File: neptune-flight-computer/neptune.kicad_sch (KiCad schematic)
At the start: 0 parts

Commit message: Continued work on board
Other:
- sheet RF renamed Data management
- added sheet STM32 (STM32.kicad_sch)
- added sheet Sensors (Sensors.kicad_sch)
- sheet Data management: file RF.kicad_sch -> data_management.kicad_sch

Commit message: Added oscillator, setup sensor SPI
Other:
- sheet Sensors ports: added CE_ACC, CE_GYR, CE_MAG, IMU_MISO, IMU_MOSI, IMU_SCK; removed BMX_Int_1, SCL, SDA
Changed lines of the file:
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@@
 (kicad_sch (version 20211123) (generator eeschema)
   (paper "A4")
+  (wire (pts (xy 241.3 35.56) (xy 245.11 35.56))
+    (stroke (width 0) (type default) (color 0 0 0 0))
+  )
+  (wire (pts (xy 241.3 46.99) (xy 245.11 46.99))
+    (stroke (width 0) (type default) (color 0 0 0 0))
+  )
+  (wire (pts (xy 241.3 50.8) (xy 245.11 50.8))
+    (stroke (width 0) (type default) (color 0 0 0 0))
+  )
+  (wire (pts (xy 241.3 39.37) (xy 245.11 39.37))
+    (stroke (width 0) (type default) (color 0 0 0 0))
+  )
+  (wire (pts (xy 241.3 43.18) (xy 245.11 43.18))
+    (stroke (width 0) (type default) (color 0 0 0 0))
+  )
+  (wire (pts (xy 241.3 31.75) (xy 245.11 31.75))
+    (stroke (width 0) (type default) (color 0 0 0 0))
+  )
+  (label "IMU_SCK" (at 245.11 50.8 0)
+    (effects (font (size 1.27 1.27)) (justify left bottom))
+  )
+  (label "CE_ACC" (at 245.11 35.56 0)
+    (effects (font (size 1.27 1.27)) (justify left bottom))
+  )
+  (label "IMU_MISO" (at 245.11 43.18 0)
+    (effects (font (size 1.27 1.27)) (justify left bottom))
+  )
+  (label "IMU_MOSI" (at 245.11 46.99 0)
+    (effects (font (size 1.27 1.27)) (justify left bottom))
+  )
+  (label "CE_MAG" (at 245.11 39.37 0)
+    (effects (font (size 1.27 1.27)) (justify left bottom))
+  )
+  (label "CE_GYR" (at 245.11 31.75 0)
+    (effects (font (size 1.27 1.27)) (justify left bottom))
+  )
   (sheet (at 25.4 88.9) (size 63.5 50.8) (fields_autoplaced)
     (stroke (width 0.1524) (type solid) (color 0 0 0 0))
@@
       (effects (font (size 1.27 1.27)) (justify left top))
     )
-    (pin "SCL" input (at 241.3 33.02 0)
-      (effects (font (size 1.27 1.27)) (justify right))
-    )
-    (pin "SDA" input (at 241.3 36.83 0)
-      (effects (font (size 1.27 1.27)) (justify right))
-    )
-    (pin "BMX_Int_1" input (at 241.3 40.64 0)
+    (pin "CE_GYR" input (at 241.3 31.75 0)
+      (effects (font (size 1.27 1.27)) (justify right))
+    )
+    (pin "CE_ACC" input (at 241.3 35.56 0)
+      (effects (font (size 1.27 1.27)) (justify right))
+    )
+    (pin "CE_MAG" input (at 241.3 39.37 0)
+      (effects (font (size 1.27 1.27)) (justify right))
+    )
+    (pin "IMU_MISO" output (at 241.3 43.18 0)
+      (effects (font (size 1.27 1.27)) (justify right))
+    )
+    (pin "IMU_SCK" input (at 241.3 50.8 0)
+      (effects (font (size 1.27 1.27)) (justify right))
+    )
+    (pin "IMU_MOSI" input (at 241.3 46.99 0)
       (effects (font (size 1.27 1.27)) (justify right))
     )
@@
       (reference "#PWR?") (unit 1) (value "GND") (footprint "")
     )
+    (path "/708c8a34-f258-4554-8b50-7818f1e46fec/1c76a57f-6fd0-487a-a4ef-6ad233efc7a4"
+      (reference "#PWR?") (unit 1) (value "GND") (footprint "")
+    )
     (path "/b694d9b6-8e2a-4217-a81b-e156ec88b46a/1e295ccf-d58f-4d56-9b3f-857eee3b562a"
       (reference "#PWR?") (unit 1) (value "GND") (footprint "")
@@
       (reference "#PWR?") (unit 1) (value "GND") (footprint "")
     )
+    (path "/708c8a34-f258-4554-8b50-7818f1e46fec/49ef88cf-fbc5-444e-b0de-982ad307474e"
+      (reference "#PWR?") (unit 1) (value "+5V") (footprint "")
+    )
+    (path "/708c8a34-f258-4554-8b50-7818f1e46fec/4b6825c9-a1f7-4ead-9756-29ea3c3b647a"
+      (reference "#PWR?") (unit 1) (value "GND") (footprint "")
+    )
     (path "/708c8a34-f258-4554-8b50-7818f1e46fec/60e7330f-4ecb-47a7-a6a7-dc5a9900bcfe"
       (reference "#PWR?") (unit 1) (value "+3.3V") (footprint "")
@@
       (reference "#PWR?") (unit 1) (value "GND") (footprint "")
     )
+    (path "/fd0daead-056b-49b0-b136-e76d44737a4c/64ccf757-c39c-4a22-ae39-be2ebf19a906"
+      (reference "#PWR?") (unit 1) (value "GND") (footprint "")
+    )
     (path "/fd0daead-056b-49b0-b136-e76d44737a4c/68003f26-a4e5-4ffc-8df9-5c391f729a97"
       (reference "#PWR?") (unit 1) (value "+3.3V") (footprint "")
@@
       (reference "#PWR?") (unit 1) (value "GND") (footprint "")
     )
-    (path "/fd0daead-056b-49b0-b136-e76d44737a4c/9780d6ee-b4a2-44ea-907d-1bb30473759e"
+    (path "/708c8a34-f258-4554-8b50-7818f1e46fec/a23244bc-53f6-42d4-9bec-2b4f35d62696"
       (reference "#PWR?") (unit 1) (value "GND") (footprint "")
     )
     (path "/761c8e29-382a-475c-a37a-7201cc9cd0f5/a470ca0b-2a36-4daa-901d-3247fe3e860c"
+      (reference "#PWR?") (unit 1) (value "GND") (footprint "")
+    )
+    (path "/708c8a34-f258-4554-8b50-7818f1e46fec/a51b5ced-5450-4509-900e-2b4a4f5469b4"
       (reference "#PWR?") (unit 1) (value "GND") (footprint "")
     )
@@
       (reference "#PWR?") (unit 1) (value "GND") (footprint "")
     )
+    (path "/708c8a34-f258-4554-8b50-7818f1e46fec/ce55234b-9d12-40d9-8108-46d3eb66f17c"
+      (reference "#PWR?") (unit 1) (value "+5V") (footprint "")
+    )
     (path "/761c8e29-382a-475c-a37a-7201cc9cd0f5/d2a988e4-3734-4b36-a333-4fd6c96f76ed"
       (reference "#PWR?") (unit 1) (value "VBUS") (footprint "")
@@
       (reference "#PWR?") (unit 1) (value "GND") (footprint "")
     )
-    (path "/fd0daead-056b-49b0-b136-e76d44737a4c/d8e3e689-c509-4bd8-b960-1bb37ee4f3bd"
-      (reference "#PWR?") (unit 1) (value "GND") (footprint "")
-    )
     (path "/708c8a34-f258-4554-8b50-7818f1e46fec/dcce9beb-a6a5-4ab2-8739-7a753559b830"
       (reference "#PWR?") (unit 1) (value "VBUS") (footprint "")
@@
       (reference "C?") (unit 1) (value "8.2n") (footprint "Capacitor_SMD:C_0402_1005Metric")
     )
+    (path "/708c8a34-f258-4554-8b50-7818f1e46fec/86e4c295-0c0b-45dc-a306-ca91d6b44a72"
+      (reference "C?") (unit 1) (value "33p") (footprint "Capacitor_SMD:C_0402_1005Metric")
+    )
     (path "/761c8e29-382a-475c-a37a-7201cc9cd0f5/877c3fb5-6549-4ea3-9af6-a23063a08a80"
       (reference "C?") (unit 1) (value "10u") (footprint "Capacitor_SMD:C_0805_2012Metric_Pad1.18x1.45mm_HandSolder")
     )
+    (path "/708c8a34-f258-4554-8b50-7818f1e46fec/9e179446-9863-4cc8-a0d5-4367254f4d3e"
+      (reference "C?") (unit 1) (value "33p") (footprint "Capacitor_SMD:C_0402_1005Metric")
+    )
     (path "/761c8e29-382a-475c-a37a-7201cc9cd0f5/bf1a3858-9fb0-46de-bab4-bd386edc9d50"
       (reference "C?") (unit 1) (value "1u") (footprint "Capacitor_SMD:C_0402_1005Metric")
@@
       (reference "J?") (unit 1) (value "Conn_Coaxial") (footprint "Connector_Coaxial:SMA_Amphenol_132291_Vertical")
     )
+    (path "/708c8a34-f258-4554-8b50-7818f1e46fec/b33b18f8-aa94-4a60-bf88-916bdc3ca6d3"
+      (reference "J?") (unit 1) (value "Conn_01x04") (footprint "Connector_PinHeader_2.54mm:PinHeader_1x04_P2.54mm_Vertical")
+    )
+    (path "/708c8a34-f258-4554-8b50-7818f1e46fec/c58efe95-928d-4eed-a2d1-8d8e37e3e668"
+      (reference "J?") (unit 1) (value "Conn_01x04") (footprint "Connector_PinHeader_2.54mm:PinHeader_1x04_P2.54mm_Vertical")
+    )
     (path "/708c8a34-f258-4554-8b50-7818f1e46fec/c6de421b-8d8f-4889-9433-957986658d20"
-      (reference "J?") (unit 1) (value "Conn_01x04") (footprint "footprints:JST_SM04B-GHS-TB(LF)(SN)-")
+      (reference "J?") (unit 1) (value "Conn_01x04") (footprint "Connector_PinHeader_2.54mm:PinHeader_1x04_P2.54mm_Vertical")
     )
     (path "/761c8e29-382a-475c-a37a-7201cc9cd0f5/d8f6b77f-bde2-4824-b9e2-53c92a41d9c6"
@@
       (reference "U?") (unit 3) (value "LM393") (footprint "footprints:SOIC127P600X175-8N")
     )
-  )
+    (path "/708c8a34-f258-4554-8b50-7818f1e46fec/16719f82-68bb-4f6d-a5e9-cdc1fab5beb3"
+      (reference "Y?") (unit 1) (value "Crystal") (footprint "Crystal:Crystal_SMD_HC49-SD")
+    )
+  )

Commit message: Continued pcb work
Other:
- sheet Data management ports: added CLK_SD, CS_RF, CS_SD, MISO_RF, MISO_SD, MOSI_RF, MOSI_SD, RESET_RF, RF_IO0, SCK_RF; removed none
- sheet STM32 ports: added CE_ACC, CE_GYR, CE_MAG, CLK_SD, CS_RF, CS_SD, IMU_MISO, IMU_MOSI, IMU_SCK, MISO_RF, MISO_SD, MOSI_RF, MOSI_SD, RESET_RF, RF_100, SCK_RF; removed none

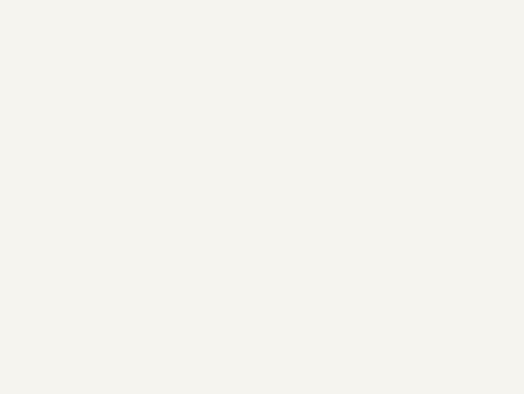
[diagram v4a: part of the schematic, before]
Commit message: Added mounting holes
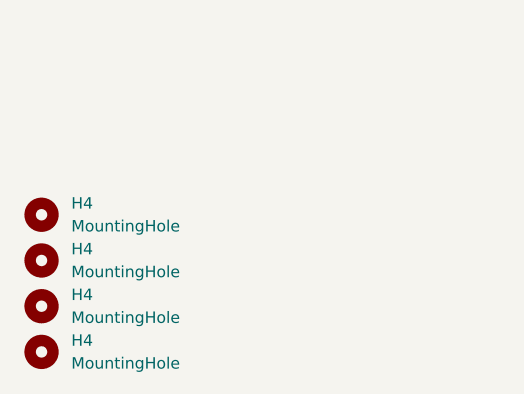
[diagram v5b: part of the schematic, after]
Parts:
- added H4 (x4): MountingHole, MountingHole:MountingHole_3.2mm_M3, symbol Mechanical:MountingHole
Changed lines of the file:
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@@
     (effects (font (size 1.27 1.27)) (justify left bottom))
+  )
+  (symbol (lib_id "Mechanical:MountingHole") (at 27.94 175.26 0) (unit 1)
+    (in_bom yes) (on_board yes) (dnp no) (fields_autoplaced)
+    (property "Reference" "H4" (at 31.242 173.9899 0)
+      (effects (font (size 1.27 1.27)) (justify left))
+    )
+    (property "Value" "MountingHole" (at 31.242 176.5299 0)
+      (effects (font (size 1.27 1.27)) (justify left))
+    )
+    (property "Footprint" "MountingHole:MountingHole_3.2mm_M3" (at 27.94 175.26 0)
+      (effects (font (size 1.27 1.27)) hide)
+    )
+    (property "Datasheet" "~" (at 27.94 175.26 0)
+      (effects (font (size 1.27 1.27)) hide)
+    )
+    (instances
+      (project "Liaka_V3"
+        (path "/9186fd02-f30d-4e17-aa38-378ab73e3908"
+          (reference "H4") (unit 1)
+        )
+      )
+      (project "neptune"
+        (path "/e63e39d7-6ac0-4ffd-8aa3-1841a4541b55"
+          (reference "H2") (unit 1)
+        )
+      )
+    )
+  )
+  (symbol (lib_id "Mechanical:MountingHole") (at 27.94 180.34 0) (unit 1)
+    (in_bom yes) (on_board yes) (dnp no) (fields_autoplaced)
+    (property "Reference" "H4" (at 31.242 179.0699 0)
+      (effects (font (size 1.27 1.27)) (justify left))
+    )
+    (property "Value" "MountingHole" (at 31.242 181.6099 0)
+      (effects (font (size 1.27 1.27)) (justify left))
+    )
+    (property "Footprint" "MountingHole:MountingHole_3.2mm_M3" (at 27.94 180.34 0)
+      (effects (font (size 1.27 1.27)) hide)
+    )
+    (property "Datasheet" "~" (at 27.94 180.34 0)
+      (effects (font (size 1.27 1.27)) hide)
+    )
+    (instances
+      (project "Liaka_V3"
+        (path "/9186fd02-f30d-4e17-aa38-378ab73e3908"
+          (reference "H4") (unit 1)
+        )
+      )
+      (project "neptune"
+        (path "/e63e39d7-6ac0-4ffd-8aa3-1841a4541b55"
+          (reference "H3") (unit 1)
+        )
+      )
+    )
+  )
+  (symbol (lib_id "Mechanical:MountingHole") (at 27.94 170.18 0) (unit 1)
+    (in_bom yes) (on_board yes) (dnp no) (fields_autoplaced)
+    (property "Reference" "H4" (at 31.242 168.9099 0)
+      (effects (font (size 1.27 1.27)) (justify left))
+    )
+    (property "Value" "MountingHole" (at 31.242 171.4499 0)
+      (effects (font (size 1.27 1.27)) (justify left))
+    )
+    (property "Footprint" "MountingHole:MountingHole_3.2mm_M3" (at 27.94 170.18 0)
+      (effects (font (size 1.27 1.27)) hide)
+    )
+    (property "Datasheet" "~" (at 27.94 170.18 0)
+      (effects (font (size 1.27 1.27)) hide)
+    )
+    (instances
+      (project "Liaka_V3"
+        (path "/9186fd02-f30d-4e17-aa38-378ab73e3908"
+          (reference "H4") (unit 1)
+        )
+      )
+      (project "neptune"
+        (path "/e63e39d7-6ac0-4ffd-8aa3-1841a4541b55"
+          (reference "H1") (unit 1)
+        )
+      )
+    )
+  )
+  (symbol (lib_id "Mechanical:MountingHole") (at 27.94 185.42 0) (unit 1)
+    (in_bom yes) (on_board yes) (dnp no) (fields_autoplaced)
+    (property "Reference" "H4" (at 31.242 184.1499 0)
+      (effects (font (size 1.27 1.27)) (justify left))
+    )
+    (property "Value" "MountingHole" (at 31.242 186.6899 0)
+      (effects (font (size 1.27 1.27)) (justify left))
+    )
+    (property "Footprint" "MountingHole:MountingHole_3.2mm_M3" (at 27.94 185.42 0)
+      (effects (font (size 1.27 1.27)) hide)
+    )
+    (property "Datasheet" "~" (at 27.94 185.42 0)
+      (effects (font (size 1.27 1.27)) hide)
+    )
+    (instances
+      (project "Liaka_V3"
+        (path "/9186fd02-f30d-4e17-aa38-378ab73e3908"
+          (reference "H4") (unit 1)
+        )
+      )
+      (project "neptune"
+        (path "/e63e39d7-6ac0-4ffd-8aa3-1841a4541b55"
+          (reference "H4") (unit 1)
+        )
+      )
+    )
   )
   (sheet (at 25.4 88.9) (size 63.5 50.8) (fields_autoplaced)
